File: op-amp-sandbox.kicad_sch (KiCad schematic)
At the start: 16 parts, among them J1 Conn_01x06, J2 Conn_01x04, U2 TLV2372

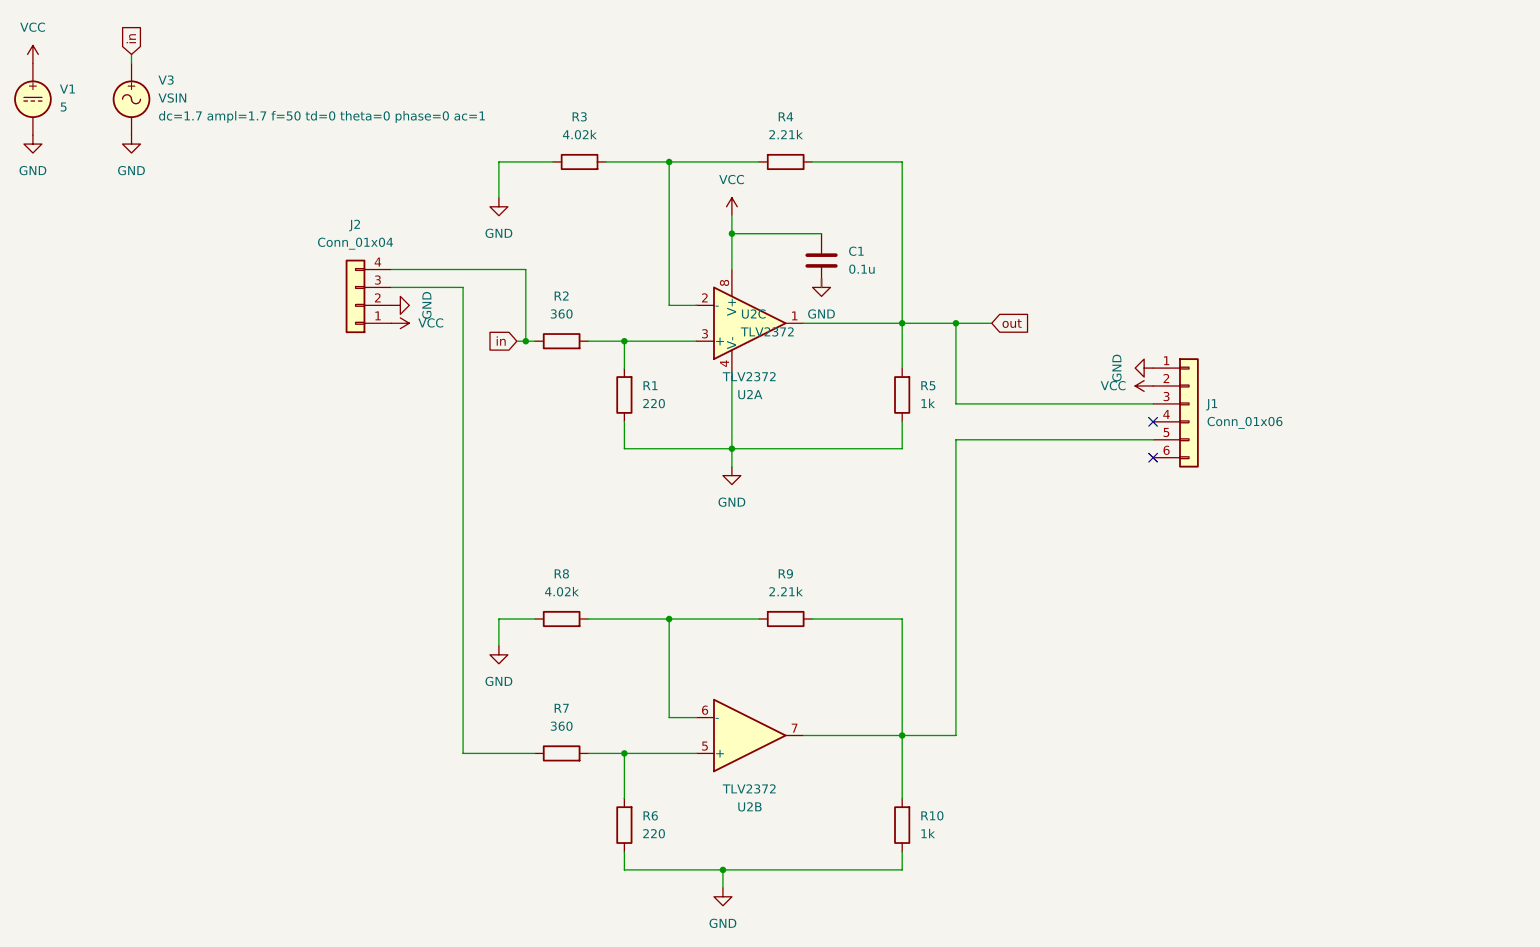
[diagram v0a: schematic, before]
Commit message: Added additional pin headers to the board.
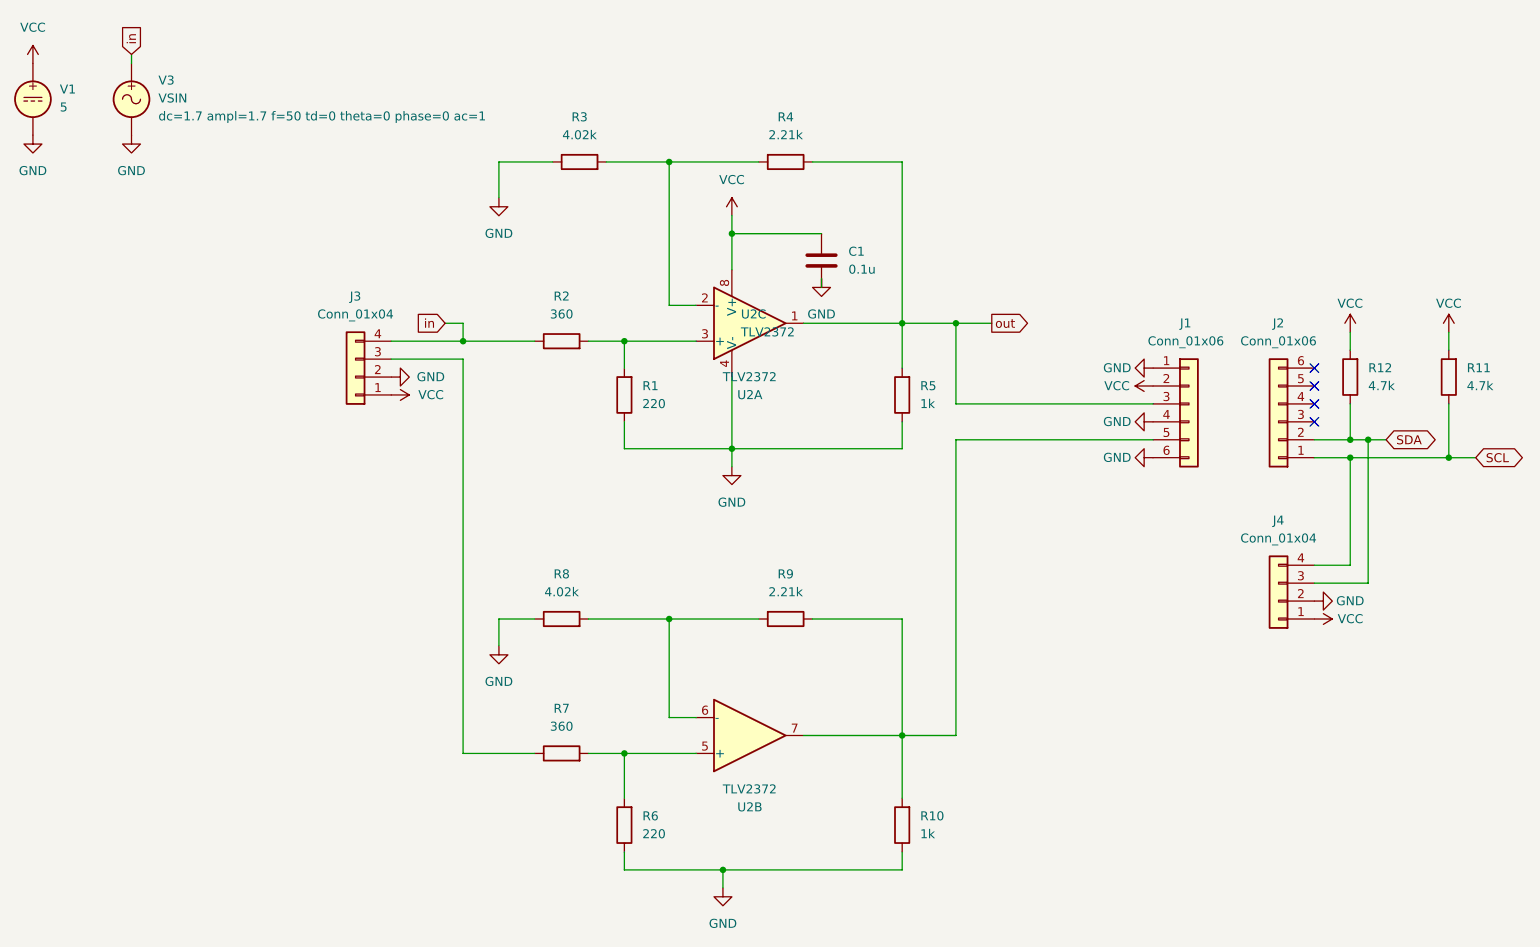
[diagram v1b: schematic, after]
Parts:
- added J2: Conn_01x06, Connector_PinSocket_2.54mm:PinSocket_1x06_P2.54mm_Vertical, symbol Connector_Generic:Conn_01x06
- added J4: Conn_01x04, Connector_PinHeader_2.54mm:PinHeader_1x04_P2.54mm_Horizontal, symbol Connector_Generic:Conn_01x04
- added R11, R12: 4.7k, Resistor_SMD:R_1206_3216Metric, symbol Device:R
- J1: footprint Connector_PinHeader_2.54mm:PinHeader_1x06_P2.54mm_Vertical -> Connector_PinSocket_2.54mm:PinSocket_1x06_P2.54mm_Vertical
- renumbered J2 to J3
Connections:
- net GND: now also J1.4 (Pin_4), J1.6 (Pin_6), J4.2 (Pin_2)
- net VCC: now also J4.1 (Pin_1), R11.2, R12.2
- new net SCL: J2.1 (Pin_1), J4.4 (Pin_4), R11.1
- new net SDA: J2.2 (Pin_2), J4.3 (Pin_3), R12.1
- no-connect marks 2 -> 4
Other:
- moved on the sheet: J3
